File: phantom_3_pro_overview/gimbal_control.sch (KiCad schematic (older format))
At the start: 0 parts

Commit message: Overview: Updated gimbal control board.
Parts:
- added U?: STM32F407IGH6, ARM-base 32-bit MCU, symbol IC_PQFP32
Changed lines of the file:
@@
 EELAYER 25 0
 EELAYER END
-$Descr A4 11693 8268
+$Descr User 5118 4803
 encoding utf-8
-Sheet 9 23
+Sheet 19 23
 Title "Overview of the Phantom 3 Pro Gimbal control"
 Date ""
@@
 Comment4 ""
 $EndDescr
+Text HLabel 1650 1950 1    60   BiDi ~ 0
+RIBBON_CENTER
+Text HLabel 3250 2300 1    60   BiDi ~ 0
+FLAT_CAMERA
+$Comp
+L IC_PQFP32 U?
+U 1 1 597AFD9A
+P 2450 1750
+F 0 "U?" H 2450 1650 50  0000 C CNN
+F 1 "STM32F407IGH6" H 2450 1850 50  0000 C CNN
+F 2 "ARM-base 32-bit MCU" H 2450 1750 50  0000 C CNN
+F 3 "DOCUMENTATION" H 2450 1750 50  0001 C CNN
+	1    2450 1750
+	1    0    0    -1
+$EndComp
+Entry Wire Line
+	3050 1400 3150 1500
+Entry Wire Line
+	3050 1500 3150 1600
+Entry Wire Line
+	3050 1600 3150 1700
+Entry Wire Line
+	3050 1700 3150 1800
+Entry Wire Line
+	3050 1800 3150 1900
+Entry Wire Line
+	3050 1900 3150 2000
+Entry Wire Line
+	3050 2000 3150 2100
+Entry Wire Line
+	3050 2100 3150 2200
+Entry Wire Line
+	2100 2350 2200 2450
+Entry Wire Line
+	2200 2350 2300 2450
+Entry Wire Line
+	2300 2350 2400 2450
+Entry Wire Line
+	2400 2350 2500 2450
+Entry Wire Line
+	2500 2350 2600 2450
+Entry Wire Line
+	2600 2350 2700 2450
+Entry Wire Line
+	2700 2350 2800 2450
+Entry Wire Line
+	2800 2350 2900 2450
+Wire Wire Line
+	2100 2350 2100 2300
+Wire Wire Line
+	2200 2300 2200 2350
+Wire Wire Line
+	2300 2350 2300 2300
+Wire Wire Line
+	2400 2300 2400 2350
+Wire Wire Line
+	2500 2350 2500 2300
+Wire Wire Line
+	2600 2300 2600 2350
+Wire Wire Line
+	2700 2350 2700 2300
+Wire Wire Line
+	2800 2300 2800 2350
+Wire Wire Line
+	3000 2100 3050 2100
+Wire Wire Line
+	3050 2000 3000 2000
+Wire Wire Line
+	3000 1900 3050 1900
+Wire Wire Line
+	3050 1800 3000 1800
+Wire Wire Line
+	3000 1700 3050 1700
+Wire Wire Line
+	3050 1600 3000 1600
+Wire Wire Line
+	3000 1500 3050 1500
+Wire Wire Line
+	3050 1400 3000 1400
+Entry Bus Bus
+	3050 2450 3150 2350
 Wire Bus Line
-	3200 2100 3900 2100
+	3150 1500 3150 2350
 Wire Bus Line
-	3250 2400 3900 2400
-Text HLabel 3900 2100 2    60   BiDi ~ 0
-RIBBON_CENTER
-Text HLabel 3900 2400 2    60   BiDi ~ 0
-FLAT_CAMERA
+	2200 2450 3050 2450
+Wire Bus Line
+	3150 2350 3250 2350
+Wire Bus Line
+	3250 2350 3250 2300
+Entry Wire Line
+	1850 2100 1750 2000
+Entry Wire Line
+	1850 2000 1750 1900
+Entry Wire Line
+	1850 1900 1750 1800
+Entry Wire Line
+	1850 1800 1750 1700
+Entry Wire Line
+	1850 1700 1750 1600
+Entry Wire Line
+	1850 1600 1750 1500
+Entry Wire Line
+	1850 1500 1750 1400
+Entry Wire Line
+	1850 1400 1750 1300
+Entry Wire Line
+	2800 1150 2700 1050
+Entry Wire Line
+	2700 1150 2600 1050
+Entry Wire Line
+	2600 1150 2500 1050
+Entry Wire Line
+	2500 1150 2400 1050
+Entry Wire Line
+	2400 1150 2300 1050
+Entry Wire Line
+	2300 1150 2200 1050
+Entry Wire Line
+	2200 1150 2100 1050
+Entry Wire Line
+	2100 1150 2000 1050
+Wire Wire Line
+	2800 1150 2800 1200
+Wire Wire Line
+	2700 1200 2700 1150
+Wire Wire Line
+	2600 1150 2600 1200
+Wire Wire Line
+	2500 1200 2500 1150
+Wire Wire Line
+	2400 1150 2400 1200
+Wire Wire Line
+	2300 1200 2300 1150
+Wire Wire Line
+	2200 1150 2200 1200
+Wire Wire Line
+	2100 1200 2100 1150
+Wire Wire Line
+	1900 1400 1850 1400
+Wire Wire Line
+	1850 1500 1900 1500
+Wire Wire Line
+	1900 1600 1850 1600
+Wire Wire Line
+	1850 1700 1900 1700
+Wire Wire Line
+	1900 1800 1850 1800
+Wire Wire Line
+	1850 1900 1900 1900
+Wire Wire Line
+	1900 2000 1850 2000
+Wire Wire Line
+	1850 2100 1900 2100
+Entry Bus Bus
+	1850 1050 1750 1150
+Wire Bus Line
+	1750 2000 1750 1150
+Wire Bus Line
+	2700 1050 1850 1050
+Wire Bus Line
+	1750 2000 1650 2000
+Wire Bus Line
+	1650 2000 1650 1950
 $EndSCHEMATC

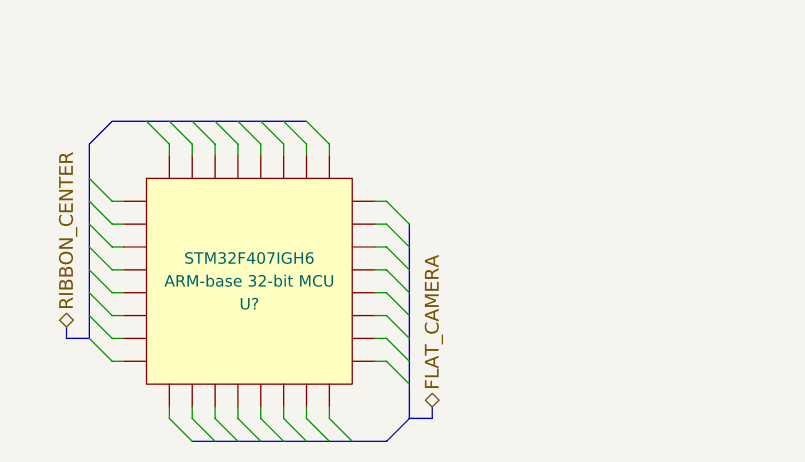
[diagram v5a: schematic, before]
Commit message: Overview: Updated to latest findings.
Added magnetometer to gimbal control, and made some minor fixes.
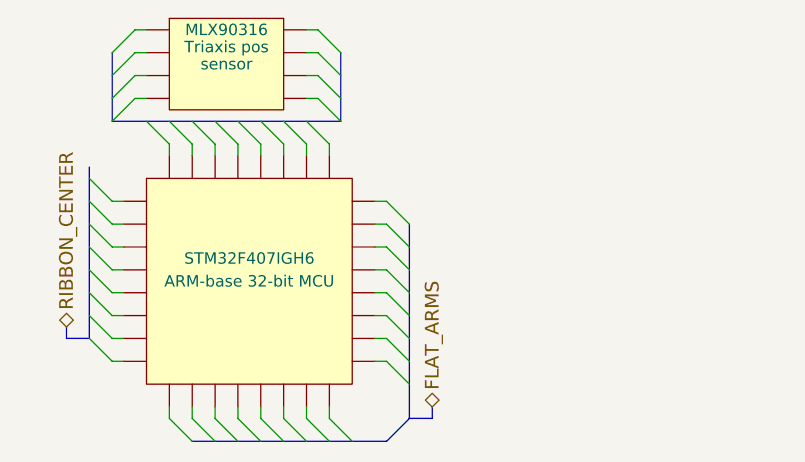
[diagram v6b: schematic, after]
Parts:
- added U?: MLX90316, Triaxis pos, symbol IC_DIL8
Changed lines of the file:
@@
 RIBBON_CENTER
 Text HLabel 3250 2300 1    60   BiDi ~ 0
-FLAT_CAMERA
+FLAT_ARMS
 $Comp
 L IC_PQFP32 U?
 U 1 1 597AFD9A
 P 2450 1750
-F 0 "U?" H 2450 1650 50  0000 C CNN
+F 0 "U?" H 2450 1650 50  0001 C CNN
 F 1 "STM32F407IGH6" H 2450 1850 50  0000 C CNN
 F 2 "ARM-base 32-bit MCU" H 2450 1750 50  0000 C CNN
@@
 Entry Wire Line
 	2800 2350 2900 2450
-Wire Wire Line
-	2100 2350 2100 2300
-Wire Wire Line
-	2200 2300 2200 2350
-Wire Wire Line
-	2300 2350 2300 2300
-Wire Wire Line
-	2400 2300 2400 2350
-Wire Wire Line
-	2500 2350 2500 2300
-Wire Wire Line
-	2600 2300 2600 2350
-Wire Wire Line
-	2700 2350 2700 2300
-Wire Wire Line
-	2800 2300 2800 2350
-Wire Wire Line
-	3000 2100 3050 2100
-Wire Wire Line
-	3050 2000 3000 2000
-Wire Wire Line
-	3000 1900 3050 1900
-Wire Wire Line
-	3050 1800 3000 1800
-Wire Wire Line
-	3000 1700 3050 1700
-Wire Wire Line
-	3050 1600 3000 1600
-Wire Wire Line
-	3000 1500 3050 1500
-Wire Wire Line
-	3050 1400 3000 1400
 Entry Bus Bus
 	3050 2450 3150 2350
+Entry Wire Line
+	1850 2100 1750 2000
+Entry Wire Line
+	1850 2000 1750 1900
+Entry Wire Line
+	1850 1900 1750 1800
+Entry Wire Line
+	1850 1800 1750 1700
+Entry Wire Line
+	1850 1700 1750 1600
+Entry Wire Line
+	1850 1600 1750 1500
+Entry Wire Line
+	1850 1500 1750 1400
+Entry Wire Line
+	1850 1400 1750 1300
+Entry Wire Line
+	2800 1150 2700 1050
+Entry Wire Line
+	2700 1150 2600 1050
+Entry Wire Line
+	2600 1150 2500 1050
+Entry Wire Line
+	2500 1150 2400 1050
+Entry Wire Line
+	2400 1150 2300 1050
+Entry Wire Line
+	2300 1150 2200 1050
+Entry Wire Line
+	2200 1150 2100 1050
+Entry Wire Line
+	2100 1150 2000 1050
+$Comp
+L IC_DIL8 U?
+U 1 1 59E16227
+P 2350 800
+F 0 "U?" H 2350 650 50  0001 C CNN
+F 1 "MLX90316" H 2350 950 50  0000 C CNN
+F 2 "Triaxis pos" H 2350 875 50  0000 C CNN
+F 3 "sensor" H 2350 800 50  0000 C CNN
+	1    2350 800
+	1    0    0    -1
+$EndComp
+Entry Wire Line
+	1850 750  1950 650
+Entry Wire Line
+	1850 850  1950 750
+Entry Wire Line
+	1850 950  1950 850
+Entry Wire Line
+	1850 1050 1950 950
+Wire Bus Line
+	1850 1050 2850 1050
+Wire Bus Line
+	1850 1050 1850 750
+Wire Bus Line
+	1750 2000 1750 1250
+Wire Bus Line
+	1650 2000 1650 1950
+Wire Bus Line
+	1750 2000 1650 2000
+Wire Wire Line
+	1850 2100 1900 2100
+Wire Wire Line
+	1900 2000 1850 2000
+Wire Wire Line
+	1850 1900 1900 1900
+Wire Wire Line
+	1900 1800 1850 1800
+Wire Wire Line
+	1850 1700 1900 1700
+Wire Wire Line
+	1900 1600 1850 1600
+Wire Wire Line
+	1850 1500 1900 1500
+Wire Wire Line
+	1900 1400 1850 1400
+Wire Wire Line
+	2100 1200 2100 1150
+Wire Wire Line
+	2200 1150 2200 1200
+Wire Wire Line
+	2300 1200 2300 1150
+Wire Wire Line
+	2400 1150 2400 1200
+Wire Wire Line
+	2500 1200 2500 1150
+Wire Wire Line
+	2600 1150 2600 1200
+Wire Wire Line
+	2700 1200 2700 1150
+Wire Wire Line
+	2800 1150 2800 1200
+Wire Bus Line
+	3250 2350 3250 2300
+Wire Bus Line
+	3150 2350 3250 2350
+Wire Bus Line
+	2200 2450 3050 2450
 Wire Bus Line
 	3150 1500 3150 2350
-Wire Bus Line
-	2200 2450 3050 2450
-Wire Bus Line
-	3150 2350 3250 2350
-Wire Bus Line
-	3250 2350 3250 2300
-Entry Wire Line
-	1850 2100 1750 2000
-Entry Wire Line
-	1850 2000 1750 1900
-Entry Wire Line
-	1850 1900 1750 1800
-Entry Wire Line
-	1850 1800 1750 1700
-Entry Wire Line
-	1850 1700 1750 1600
-Entry Wire Line
-	1850 1600 1750 1500
-Entry Wire Line
-	1850 1500 1750 1400
-Entry Wire Line
-	1850 1400 1750 1300
-Entry Wire Line
-	2800 1150 2700 1050
-Entry Wire Line
-	2700 1150 2600 1050
-Entry Wire Line
-	2600 1150 2500 1050
-Entry Wire Line
-	2500 1150 2400 1050
-Entry Wire Line
-	2400 1150 2300 1050
-Entry Wire Line
-	2300 1150 2200 1050
-Entry Wire Line
-	2200 1150 2100 1050
-Entry Wire Line
-	2100 1150 2000 1050
-Wire Wire Line
-	2800 1150 2800 1200
-Wire Wire Line
-	2700 1200 2700 1150
-Wire Wire Line
-	2600 1150 2600 1200
-Wire Wire Line
-	2500 1200 2500 1150
-Wire Wire Line
-	2400 1150 2400 1200
-Wire Wire Line
-	2300 1200 2300 1150
-Wire Wire Line
-	2200 1150 2200 1200
-Wire Wire Line
-	2100 1200 2100 1150
-Wire Wire Line
-	1900 1400 1850 1400
-Wire Wire Line
-	1850 1500 1900 1500
-Wire Wire Line
-	1900 1600 1850 1600
-Wire Wire Line
-	1850 1700 1900 1700
-Wire Wire Line
-	1900 1800 1850 1800
-Wire Wire Line
-	1850 1900 1900 1900
-Wire Wire Line
-	1900 2000 1850 2000
-Wire Wire Line
-	1850 2100 1900 2100
-Entry Bus Bus
-	1850 1050 1750 1150
-Wire Bus Line
-	1750 2000 1750 1150
-Wire Bus Line
-	2700 1050 1850 1050
-Wire Bus Line
-	1750 2000 1650 2000
-Wire Bus Line
-	1650 2000 1650 1950
+Wire Wire Line
+	3050 1400 3000 1400
+Wire Wire Line
+	3000 1500 3050 1500
+Wire Wire Line
+	3050 1600 3000 1600
+Wire Wire Line
+	3000 1700 3050 1700
+Wire Wire Line
+	3050 1800 3000 1800
+Wire Wire Line
+	3000 1900 3050 1900
+Wire Wire Line
+	3050 2000 3000 2000
+Wire Wire Line
+	3000 2100 3050 2100
+Wire Wire Line
+	2800 2300 2800 2350
+Wire Wire Line
+	2700 2350 2700 2300
+Wire Wire Line
+	2600 2300 2600 2350
+Wire Wire Line
+	2500 2350 2500 2300
+Wire Wire Line
+	2400 2300 2400 2350
+Wire Wire Line
+	2300 2350 2300 2300
+Wire Wire Line
+	2200 2300 2200 2350
+Wire Wire Line
+	2100 2350 2100 2300
+Wire Wire Line
+	1950 650  2000 650
+Wire Wire Line
+	2000 750  1950 750
+Wire Wire Line
+	1950 850  2000 850
+Wire Wire Line
+	2000 950  1950 950
+Entry Wire Line
+	2850 750  2750 650
+Entry Wire Line
+	2850 850  2750 750
+Entry Wire Line
+	2850 950  2750 850
+Entry Wire Line
+	2850 1050 2750 950
+Wire Bus Line
+	2850 1050 2850 750
+Wire Wire Line
+	2750 650  2700 650
+Wire Wire Line
+	2700 750  2750 750
+Wire Wire Line
+	2750 850  2700 850
+Wire Wire Line
+	2700 950  2750 950
 $EndSCHEMATC

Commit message: Overview: Separated gimbal power circuit.
This is to make sure the connection won't be interpreted as data link.
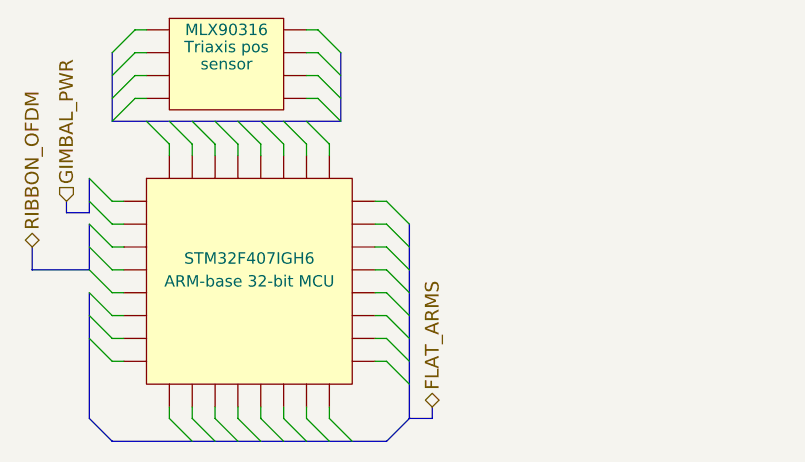
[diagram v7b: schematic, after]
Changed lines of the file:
@@
 $Descr User 5118 4803
 encoding utf-8
-Sheet 19 23
+Sheet 19 24
 Title "Overview of the Phantom 3 Pro Gimbal control"
 Date ""
@@
 Comment4 ""
 $EndDescr
-Text HLabel 1650 1950 1    60   BiDi ~ 0
-RIBBON_CENTER
+Text HLabel 1650 1400 1    60   Input ~ 0
+GIMBAL_PWR
 Text HLabel 3250 2300 1    60   BiDi ~ 0
 FLAT_ARMS
@@
 	1850 1050 1850 750
 Wire Bus Line
-	1750 2000 1750 1250
-Wire Bus Line
-	1650 2000 1650 1950
-Wire Bus Line
-	1750 2000 1650 2000
+	1650 1450 1650 1400
+Wire Bus Line
+	1750 1450 1650 1450
 Wire Wire Line
 	1850 2100 1900 2100
@@
 	3150 2350 3250 2350
 Wire Bus Line
-	2200 2450 3050 2450
+	1850 2450 3050 2450
 Wire Bus Line
 	3150 1500 3150 2350
@@
 Wire Wire Line
 	2700 950  2750 950
+Wire Bus Line
+	1750 1450 1750 1300
+Entry Bus Bus
+	1750 2350 1850 2450
+Text HLabel 1500 1600 1    60   BiDi ~ 0
+RIBBON_OFDM
+Wire Bus Line
+	1500 1600 1500 1700
+Wire Bus Line
+	1500 1700 1750 1700
+Wire Bus Line
+	1750 1700 1750 1500
+Wire Bus Line
+	1750 1800 1750 2350
 $EndSCHEMATC

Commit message: Overview: Upgraded to KiCAD 5.0.1.
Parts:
- U?: symbol IC_PQFP32 -> ic_dil_generic:IC_PQFP32
- U?: symbol IC_DIL8 -> ic_dil_generic:IC_DIL8
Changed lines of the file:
@@
-EESchema Schematic File Version 2
-LIBS:power
-LIBS:device
-LIBS:transistors
-LIBS:conn
-LIBS:linear
-LIBS:regul
-LIBS:74xx
-LIBS:cmos4000
-LIBS:adc-dac
-LIBS:memory
-LIBS:xilinx
-LIBS:microcontrollers
-LIBS:dsp
-LIBS:microchip
-LIBS:analog_switches
-LIBS:motorola
-LIBS:texas
-LIBS:intel
-LIBS:audio
-LIBS:interface
-LIBS:digital-audio
-LIBS:philips
-LIBS:display
-LIBS:cypress
-LIBS:siliconi
-LIBS:opto
-LIBS:atmel
-LIBS:contrib
-LIBS:valves
-LIBS:motors
-LIBS:ic_dil_generic
-LIBS:sensors
-LIBS:u-blox
-LIBS:amplifiers
-LIBS:transistors-switches
-LIBS:transistors-power
-LIBS:sensors-v2
-LIBS:regul-v2
+EESchema Schematic File Version 4
 LIBS:phantom_3_pro_overview-cache
-EELAYER 25 0
+EELAYER 26 0
 EELAYER END
 $Descr User 5118 4803
@@
 FLAT_ARMS
 $Comp
-L IC_PQFP32 U?
+L ic_dil_generic:IC_PQFP32 U?
 U 1 1 597AFD9A
 P 2450 1750
@@
 	2100 1150 2000 1050
 $Comp
-L IC_DIL8 U?
+L ic_dil_generic:IC_DIL8 U?
 U 1 1 59E16227
 P 2350 800
